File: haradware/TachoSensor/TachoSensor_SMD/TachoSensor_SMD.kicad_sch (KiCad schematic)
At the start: 6 parts, among them J101 OUT, U101 RPR-220

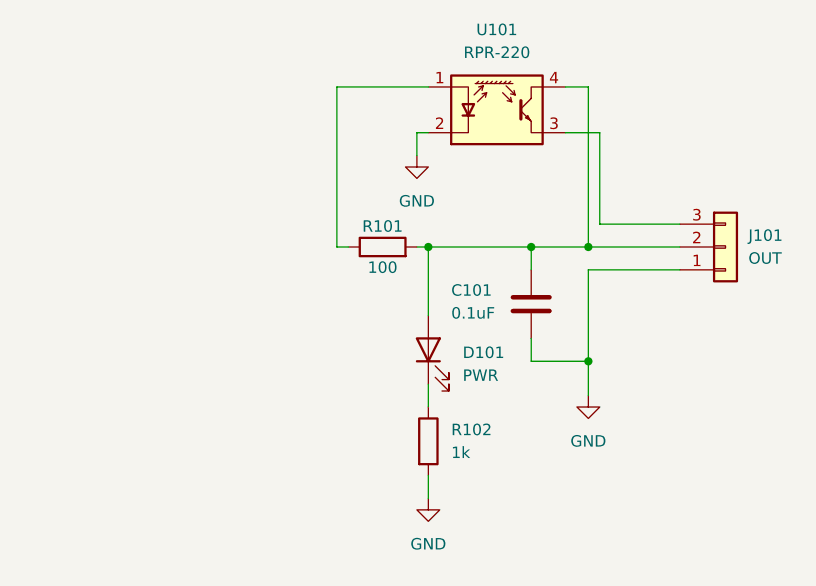
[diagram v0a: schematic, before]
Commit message: SMDタイプの設計．PWRLEDを追加
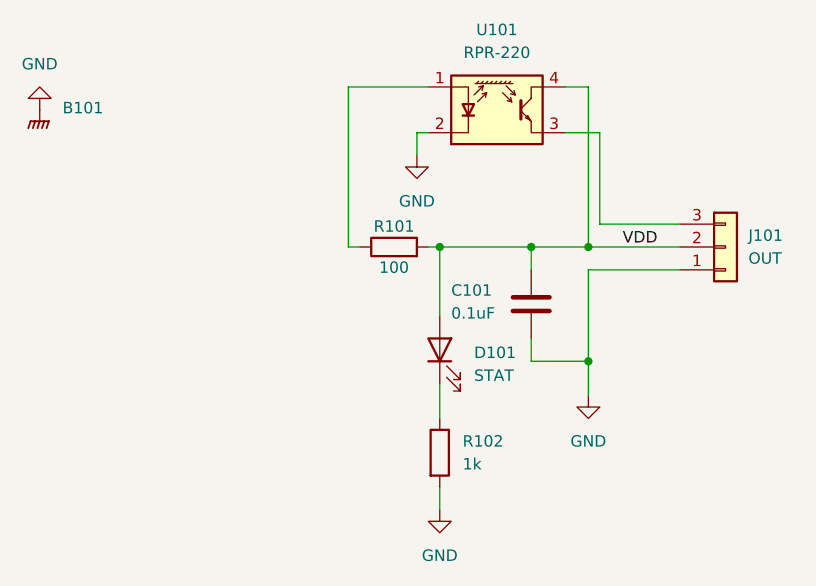
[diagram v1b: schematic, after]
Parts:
- added B101: ~, WOBCLibrary:Board_1U_60x60, symbol WOBCLibrary:Board
- C101: footprint Capacitor_THT:C_Disc_D5.0mm_W2.5mm_P2.50mm -> Capacitor_SMD:C_0402_1005Metric
- D101: value PWR -> STAT; footprint LED_SMD:LED_0603_1608Metric_Pad1.05x0.95mm_HandSolder -> LED_SMD:LED_0805_2012Metric
- R101: footprint Resistor_THT:R_Axial_DIN0207_L6.3mm_D2.5mm_P10.16mm_Horizontal -> Resistor_SMD:R_0805_2012Metric
- R102: footprint Resistor_THT:R_Axial_DIN0207_L6.3mm_D2.5mm_P10.16mm_Horizontal -> Resistor_SMD:R_0402_1005Metric
- U101: footprint OptoDevice:Everlight_ITR8307F43 -> Library:RPR220
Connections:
- net GND: now also B101.GND
- net VDD: now reaches C101.1, D101.2 (A), J101.2 (Pin_2), R101.2, U101.4 (4C)
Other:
- moved on the sheet: R101
